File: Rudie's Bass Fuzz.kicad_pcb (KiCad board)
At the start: 2 copper layers, 25 x 50 mm, 15 parts, among them J1 Conn_01x01_Male, J2 Conn_01x01_Male, J3 Conn_01x01_Male, J4 Conn_01x01_Male, Q1 BC549

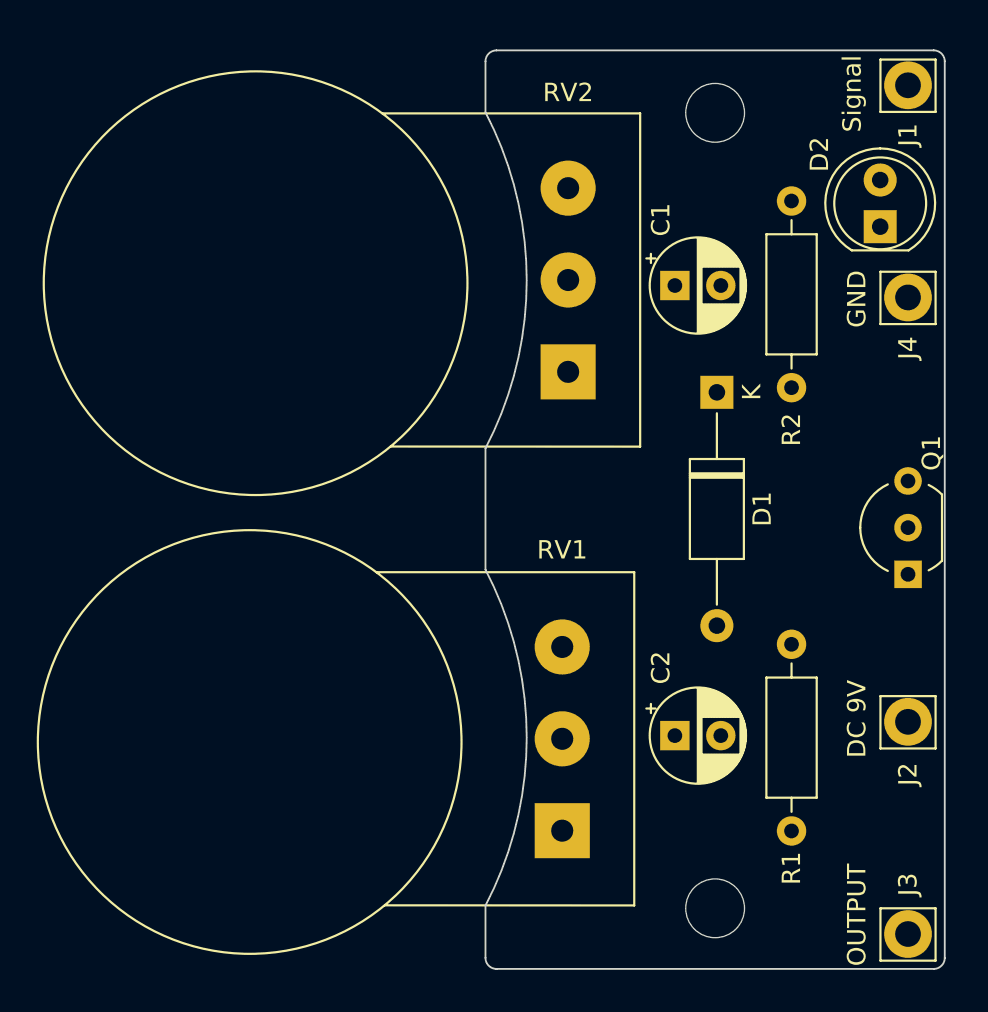
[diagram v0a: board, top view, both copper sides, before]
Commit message: Added logo's + text to Bsilk
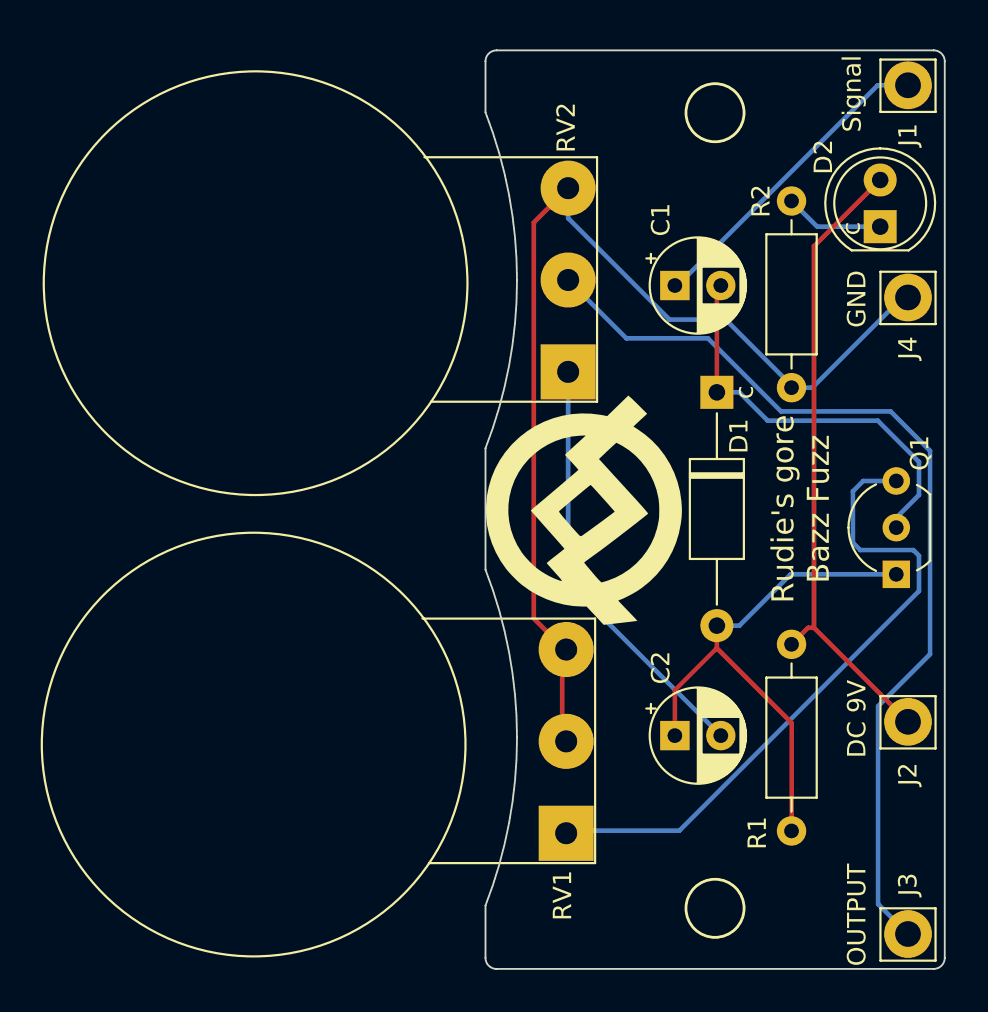
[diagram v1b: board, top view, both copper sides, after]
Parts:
- added G***: LOGO, LOGO, F.Cu at (164.2, 67.7)
- added G***: LOGO, LOGO, B.Cu at (166.5, 67.5)
- moved Q1 0.64 mm to (181.0, 71.1)
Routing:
- net GND: track 0.00 -> 57.5 mm
- net Output: track 0.00 -> 51.7 mm
- net Net-(Q1-Pad3): track 0.00 -> 35.4 mm
- net 9V: track 0.00 -> 34.7 mm
- net Net-(C2-Pad1): track 0.00 -> 29.5 mm
- net Net-(C2-Pad2): track 0.00 -> 23.2 mm
- net Net-(C1-Pad2): track 0.00 -> 22.6 mm
- net Signal: track 0.00 -> 17.2 mm
- net Net-(D2-Pad1): track 0.00 -> 5.40 mm
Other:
- board text added: "Be Nice"
- board text added: "Rudie's gore Bazz Fuzz"
- board text added: "c"

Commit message: removed wires and added extra gnd pins
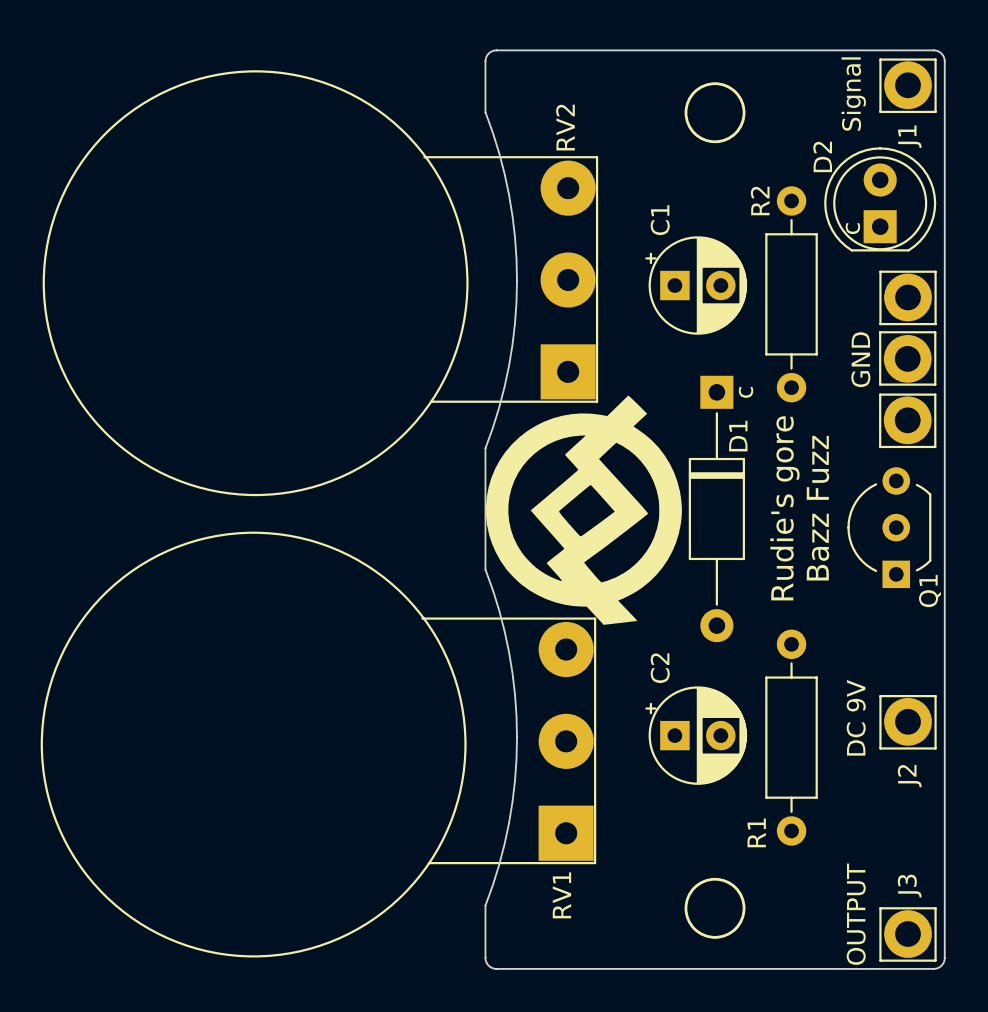
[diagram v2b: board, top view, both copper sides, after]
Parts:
- added J5: Conn_01x01_Male, Connector_Pin:Pin_D1.4mm_L8.5mm_W2.8mm_FlatFork, F.Cu at (181.6, 62.7)
- added J6: Conn_01x01_Male, Connector_Pin:Pin_D1.4mm_L8.5mm_W2.8mm_FlatFork, F.Cu at (181.6, 59.4)
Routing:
- net GND: track 57.5 -> 0.00 mm
- net Output: track 51.7 -> 0.00 mm
- net Net-(Q1-Pad3): track 35.4 -> 0.00 mm
- net 9V: track 34.7 -> 0.00 mm
- net Net-(C2-Pad1): track 29.5 -> 0.00 mm
- net Net-(C2-Pad2): track 23.2 -> 0.00 mm
- net Net-(C1-Pad2): track 22.6 -> 0.00 mm
- net Signal: track 17.2 -> 0.00 mm
- net Net-(D2-Pad1): track 5.40 -> 0.00 mm

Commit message: New wiring (ticker traces)
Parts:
- renumbered G*** to G1, G*** to G2
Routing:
- net GND: track 0.00 -> 64.4 mm
- net Output: track 0.00 -> 43.3 mm
- net 9V: track 0.00 -> 36.0 mm
- net Net-(Q1-Pad3): track 0.00 -> 30.5 mm
- net Net-(C2-Pad1): track 0.00 -> 28.1 mm
- net Net-(C2-Pad2): track 0.00 -> 23.2 mm
- net Net-(C1-Pad2): track 0.00 -> 18.7 mm
- net Signal: track 0.00 -> 18.3 mm
- net Net-(D2-Pad1): track 0.00 -> 5.40 mm
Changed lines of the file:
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@@
     (at 164.214424 67.737512 90)
     (attr board_only exclude_from_pos_files exclude_from_bom)
-    (fp_text reference "G***" (at 0 0 90) (layer "B.SilkS") hide
+    (fp_text reference "G1" (at 0 0 90) (layer "B.SilkS") hide
       (effects (font (size 1.524 1.524) (thickness 0.3)) (justify mirror))
     )
@@
     (at 166.470469 67.485836 -90)
     (attr board_only exclude_from_pos_files exclude_from_bom)
-    (fp_text reference "G***" (at 0 0 90) (layer "B.SilkS") hide
+    (fp_text reference "G2" (at 0 0 90) (layer "B.SilkS") hide
       (effects (font (size 1.524 1.524) (thickness 0.3)) (justify mirror))
     )
@@
     (effects (font (size 1 1) (thickness 0.15)))
   )
+  (segment (start 168.91 53.594) (end 178.004 44.5) (width 0.5) (layer "B.Cu") (net 1))
+  (segment (start 168.91 55.4) (end 168.91 53.594) (width 0.5) (layer "B.Cu") (net 1))
+  (segment (start 178.004 44.5) (end 181.6 44.5) (width 0.5) (layer "B.Cu") (net 1))
+  (segment (start 171.41 55.4) (end 171.196 55.614) (width 0.5) (layer "F.Cu") (net 2))
+  (segment (start 171.196 55.614) (end 171.196 61.214) (width 0.5) (layer "F.Cu") (net 2))
+  (segment (start 180.0121 68.58) (end 172.6461 61.214) (width 0.5) (layer "B.Cu") (net 2))
+  (segment (start 180.96 68.58) (end 180.0121 68.58) (width 0.5) (layer "B.Cu") (net 2))
+  (segment (start 171.196 61.214) (end 172.6461 61.214) (width 0.5) (layer "B.Cu") (net 2))
+  (segment (start 168.91 75.946) (end 170.942 73.914) (width 0.5) (layer "F.Cu") (net 3))
+  (segment (start 168.91 79.9) (end 168.91 75.946) (width 0.5) (layer "F.Cu") (net 3))
+  (segment (start 170.942 73.914) (end 171.196 73.914) (width 0.5) (layer "F.Cu") (net 3))
+  (segment (start 175.26 85.09) (end 171.45 85.09) (width 0.5) (layer "B.Cu") (net 3))
+  (segment (start 171.45 85.09) (end 168.91 82.55) (width 0.5) (layer "B.Cu") (net 3))
+  (segment (start 171.196 73.914) (end 173.99 71.12) (width 0.5) (layer "B.Cu") (net 3))
+  (segment (start 168.91 82.55) (end 168.91 79.9) (width 0.5) (layer "B.Cu") (net 3))
+  (segment (start 173.99 71.12) (end 180.96 71.12) (width 0.5) (layer "B.Cu") (net 3))
+  (segment (start 171.41 79.9) (end 171.41 79.462) (width 0.5) (layer "B.Cu") (net 4))
+  (segment (start 171.41 79.462) (end 163.1 71.152) (width 0.5) (layer "B.Cu") (net 4))
+  (segment (start 163.1 71.152) (end 163.1 60.1) (width 0.5) (layer "B.Cu") (net 4))
+  (segment (start 177.7698 72.4202) (end 175.26 74.93) (width 0.5) (layer "F.Cu") (net 5))
+  (segment (start 180.086 49.657) (end 178.943 49.657) (width 0.5) (layer "F.Cu") (net 5))
+  (segment (start 178.943 49.657) (end 177.7698 50.8302) (width 0.5) (layer "F.Cu") (net 5))
+  (segment (start 177.7698 50.8302) (end 177.7698 72.4202) (width 0.5) (layer "F.Cu") (net 5))
+  (segment (start 175.26 74.93) (end 177.38 74.93) (width 0.5) (layer "B.Cu") (net 5))
+  (segment (start 177.38 74.93) (end 181.6 79.15) (width 0.5) (layer "B.Cu") (net 5))
+  (segment (start 181.6 86.9976) (end 166.0498 71.4474) (width 0.5) (layer "B.Cu") (net 6))
+  (segment (start 181.6 90.7) (end 181.6 86.9976) (width 0.5) (layer "B.Cu") (net 6))
+  (segment (start 166.0498 71.4474) (end 166.0498 58.0498) (width 0.5) (layer "B.Cu") (net 6))
+  (segment (start 166.0498 58.0498) (end 163.1 55.1) (width 0.5) (layer "B.Cu") (net 6))
+  (segment (start 169.5477 85.2143) (end 162.9934 85.2143) (width 0.5) (layer "F.Cu") (net 7))
+  (segment (start 179.324 75.438) (end 169.5477 85.2143) (width 0.5) (layer "F.Cu") (net 7))
+  (segment (start 180.96 66.04) (end 179.324 67.676) (width 0.5) (layer "F.Cu") (net 7))
+  (segment (start 179.324 67.676) (end 179.324 75.438) (width 0.5) (layer "F.Cu") (net 7))
+  (segment (start 160.782 52.418) (end 160.782 73.0029) (width 0.5) (layer "F.Cu") (net 8))
+  (segment (start 160.782 73.0029) (end 162.9934 75.2143) (width 0.5) (layer "F.Cu") (net 8))
+  (segment (start 163.1 50.1) (end 160.782 52.418) (width 0.5) (layer "F.Cu") (net 8))
+  (segment (start 162.9934 75.2143) (end 162.9934 80.2143) (width 0.5) (layer "F.Cu") (net 8))
+  (segment (start 166.37 56.642) (end 166.37 54.61) (width 0.5) (layer "B.Cu") (net 8))
+  (segment (start 166.37 54.61) (end 163.1 51.34) (width 0.5) (layer "B.Cu") (net 8))
+  (segment (start 173.482 58.928) (end 168.656 58.928) (width 0.5) (layer "B.Cu") (net 8))
+  (segment (start 179.8066 60.96) (end 175.26 60.96) (width 0.5) (layer "B.Cu") (net 8))
+  (segment (start 168.656 58.928) (end 166.37 56.642) (width 0.5) (layer "B.Cu") (net 8))
+  (segment (start 175.26 60.706) (end 173.482 58.928) (width 0.5) (layer "B.Cu") (net 8))
+  (segment (start 163.1 51.34) (end 163.1 50.1) (width 0.5) (layer "B.Cu") (net 8))
+  (segment (start 181.5846 59.394) (end 181.5846 56.0654) (width 0.5) (layer "B.Cu") (net 8))
+  (segment (start 181.5846 62.738) (end 181.5846 59.394) (width 0.5) (layer "B.Cu") (net 8))
+  (segment (start 175.26 60.96) (end 175.26 60.706) (width 0.5) (layer "B.Cu") (net 8))
+  (segment (start 181.5846 62.738) (end 179.8066 60.96) (width 0.5) (layer "B.Cu") (net 8))
+  (segment (start 180.086 52.197) (end 176.657 52.197) (width 0.5) (layer "B.Cu") (net 9))
+  (segment (start 176.657 52.197) (end 175.26 50.8) (width 0.5) (layer "B.Cu") (net 9))
 )

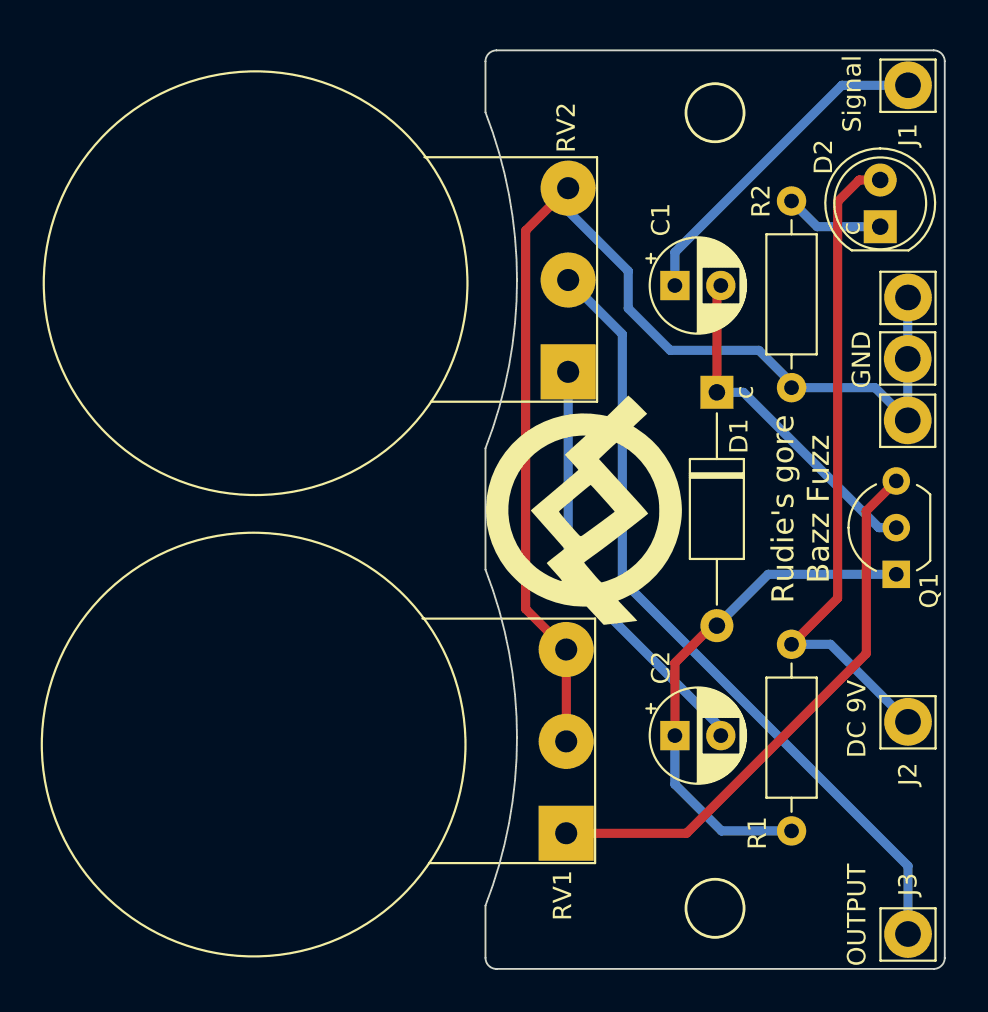
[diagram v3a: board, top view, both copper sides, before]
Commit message: Single layer PCB
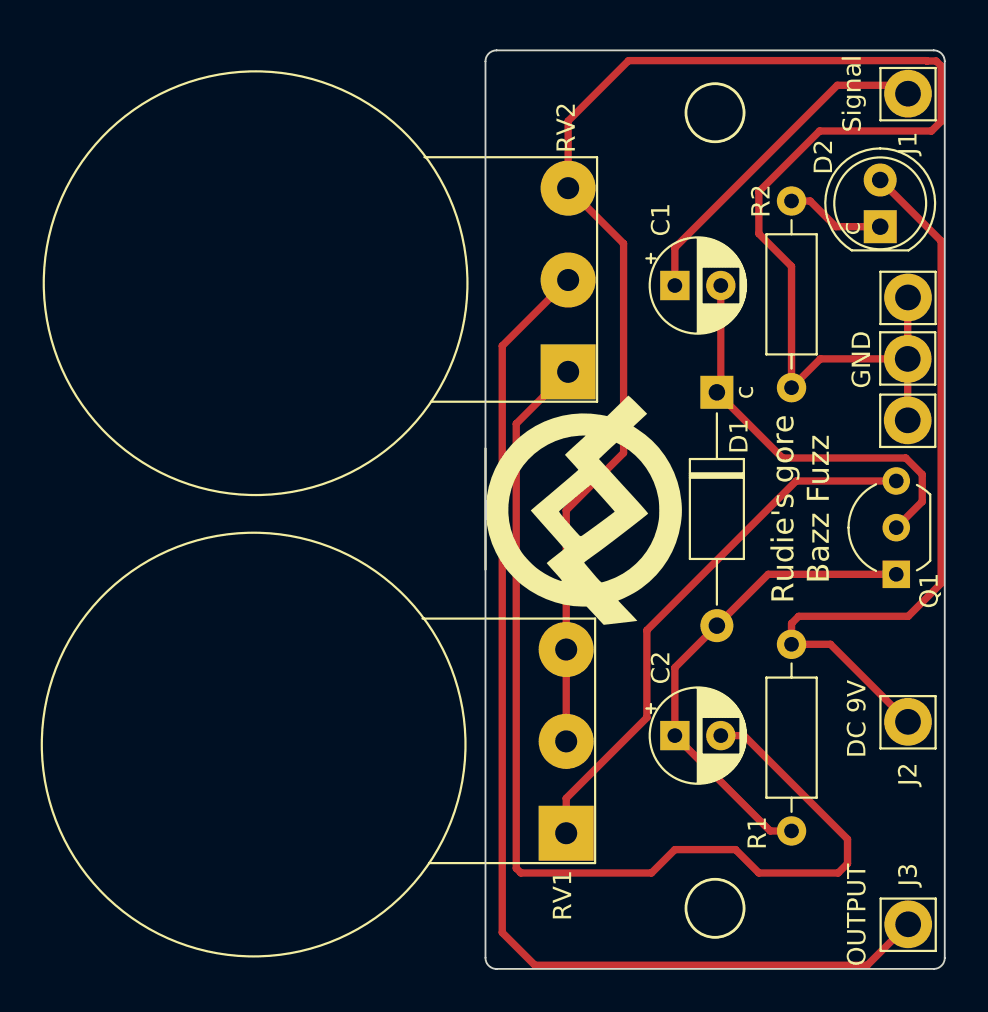
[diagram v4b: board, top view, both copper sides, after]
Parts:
- moved J3 0.53 mm to (181.6, 90.2)
- moved J1 0.46 mm to (181.6, 45.0)
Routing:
- net Net-(C2-Pad2): track 23.2 -> 58.2 mm
- net GND: track 64.4 -> 97.7 mm
- net Output: track 43.3 -> 60.8 mm
- net 9V: track 36.0 -> 41.6 mm
- net Net-(C1-Pad2): track 18.7 -> 22.4 mm
- net Net-(C2-Pad1): track 28.1 -> 26.4 mm
- net Net-(Q1-Pad3): track 30.5 -> 29.8 mm
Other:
- outline, holes or cut-outs redrawn

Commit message: V0.1 Finished
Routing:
- net Net-(Q1-Pad3): track 29.8 -> 30.9 mm
- net Output: track 60.8 -> 59.7 mm
- net Net-(C1-Pad2): track 22.4 -> 23.1 mm
- net 9V: track 41.6 -> 42.3 mm
- net GND: track 97.7 -> 98.3 mm
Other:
- outline, holes or cut-outs redrawn
- board text added: "Rudie's gore Bazz Fuzz V0.1 15-12-2022"
